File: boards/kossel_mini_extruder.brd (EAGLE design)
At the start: 66.9 x 57.9 mm, 33 parts

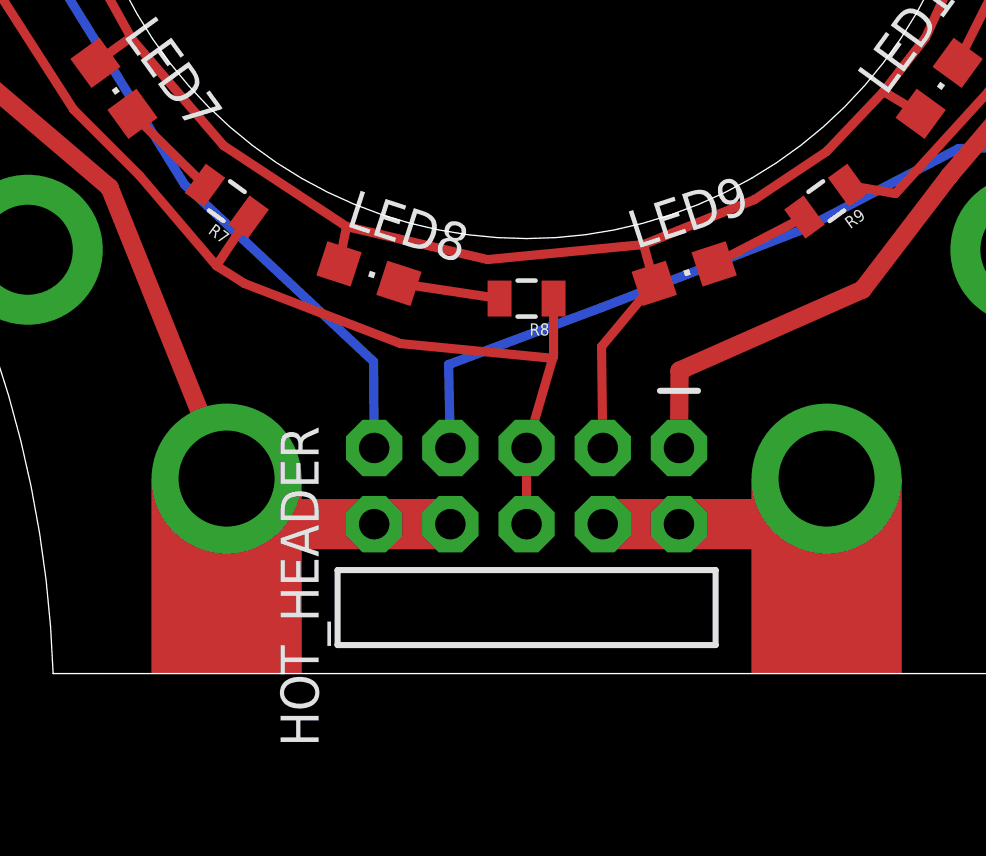
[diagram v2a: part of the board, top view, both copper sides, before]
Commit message: replaced 2x5 header with 2x4 header
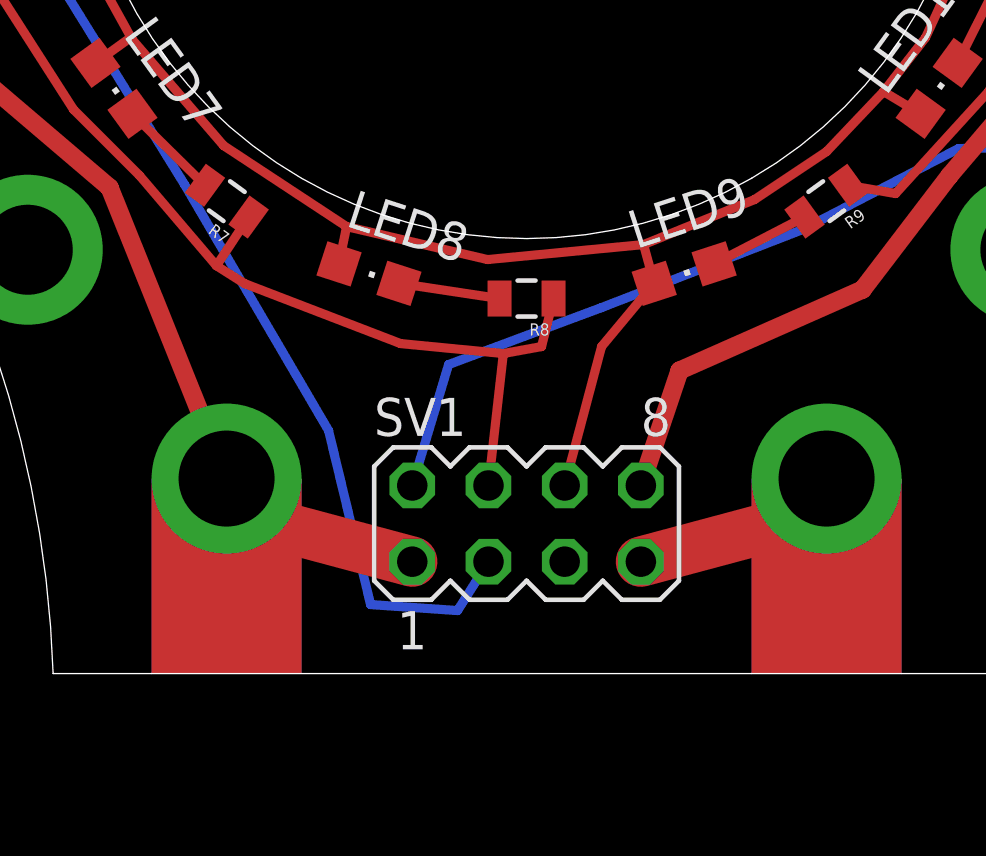
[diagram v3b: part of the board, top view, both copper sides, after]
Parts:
- removed HOT_HEADER: M05X2RA, SparkFun-Connectors:2X5-RA
- added SV1: (no value), con-lstb:MA04-2
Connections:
- net FAN_VCC: now also SV1.6; no longer HOT_HEADER.3
- net GND: now also SV1.4; no longer HOT_HEADER.5, HOT_HEADER.6
- net N$10: now also SV1.1; no longer HOT_HEADER.10, HOT_HEADER.8
- net N$11: now also SV1.3; no longer HOT_HEADER.9
- net N$12: now also SV1.2; no longer HOT_HEADER.7
- net N$15: now also SV1.7; no longer HOT_HEADER.2, HOT_HEADER.4
- net N$17: now also SV1.8; no longer HOT_HEADER.1
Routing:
- net N$11: track 49.9 -> 58.7 mm
- net GND: track 154.0 -> 152.1 mm
- net N$17: track 120.9 -> 122.4 mm
- net N$12: track 47.6 -> 49.1 mm
- net FAN_VCC: track 118.3 -> 119.7 mm
- net N$15: track 10.4 -> 9.29 mm
- net N$10: track 126.7 -> 125.5 mm
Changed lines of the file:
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@@
 <element name="R10" library="SparkFun-Passives" package="0805" value="" x="49.167959375" y="23.7467125" rot="R252"/>
 <element name="HOT_12V" library="OBKP_Effector_PCB" package="3MM" value="LUG3-X" x="23" y="6"/>
-<element name="HOT_HEADER" library="SparkFun-Connectors" package="2X5-RA" value="M05X2RA" x="33" y="5.75" rot="R270"/>
 <element name="PROBE_GND" library="OBKP_Effector_PCB" package="3MM" value="LUG3-X" x="47.9" y="49.15" rot="R120"/>
 <element name="PROBE_SIG" library="OBKP_Effector_PCB" package="3MM" value="LUG3-X" x="57.95" y="31.85" rot="R120"/>
+<element name="SV1" library="con-lstb" package="MA04-2" value="" x="33" y="4.5">
+<attribute name="OC_NEWARK" value="unknown" x="33" y="4.5" size="1.778" layer="27" display="off"/>
+<attribute name="MPN" value="" x="33" y="4.5" size="1.778" layer="27" display="off"/>
+<attribute name="MF" value="" x="33" y="4.5" size="1.778" layer="27" display="off"/>
+<attribute name="OC_FARNELL" value="unknown" x="33" y="4.5" size="1.778" layer="27" display="off"/>
+</element>
 </elements>
 <signals>
@@
 <contactref element="R8" pad="1"/>
 <contactref element="R7" pad="1"/>
-<contactref element="HOT_HEADER" pad="5"/>
-<contactref element="HOT_HEADER" pad="6"/>
 <contactref element="THERM_GND" pad="P$3"/>
 <contactref element="THERM_GND" pad="P$2"/>
@@
 <contactref element="PROBE_GND" pad="P$3"/>
 <contactref element="PROBE_GND" pad="P$2"/>
-<wire x1="33" y1="4.48" x2="33" y2="7.02" width="0.3048" layer="1"/>
-<wire x1="33" y1="7.02" x2="33.873078125" y2="10.007865625" width="0.3048" layer="1"/>
-<wire x1="33.873078125" y1="10.007865625" x2="33.9" y2="10.1" width="0.3048" layer="1"/>
-<wire x1="33.9" y1="10.1" x2="33.9" y2="12" width="0.3048" layer="1"/>
+<wire x1="33.5" y1="10.4" x2="33.9" y2="12" width="0.3048" layer="1"/>
 <wire x1="23.7357625" y1="14.717703125" x2="22.662346875" y2="13.094290625" width="0.3048" layer="1"/>
 <wire x1="22.662346875" y1="13.094290625" x2="23.6" y2="12.5" width="0.3048" layer="1"/>
 <wire x1="23.6" y1="12.5" x2="28.8" y2="10.5" width="0.3048" layer="1"/>
-<wire x1="28.8" y1="10.5" x2="33.873078125" y2="10.007865625" width="0.3048" layer="1"/>
+<wire x1="28.8" y1="10.5" x2="32.225965625" y2="10.16765" width="0.3048" layer="1"/>
 <wire x1="17.110153125" y1="22.890759375" x2="15.4" y2="22.2" width="0.3048" layer="1"/>
 <wire x1="15.4" y1="22.2" x2="17.9" y2="18.3" width="0.3048" layer="1"/>
@@
 <wire x1="8.08193125" y1="31.839365625" x2="5.267346875" y2="33.464365625" width="0.6096" layer="1"/>
 <wire x1="47.9" y1="49.15" x2="50.71458125" y2="50.775" width="0.6096" layer="1"/>
+<contactref element="SV1" pad="4"/>
+<wire x1="31.73" y1="5.77" x2="32.225965625" y2="10.16765" width="0.3048" layer="1"/>
 <wire x1="50.71458125" y1="50.775" x2="50.71458125" y2="50.775" width="0" layer="19" extent="1-16"/>
 <wire x1="5.267346875" y1="33.464365625" x2="5.267346875" y2="33.464365625" width="0" layer="19" extent="1-16"/>
+<wire x1="32.225965625" y1="10.16765" x2="33.5" y2="10.4" width="0.3048" layer="1"/>
 </signal>
 <signal name="N$7">
@@
 <contactref element="LED3" pad="A"/>
 <contactref element="LED2" pad="A"/>
-<contactref element="HOT_HEADER" pad="3"/>
 <wire x1="37.254678125" y1="12.507571875" x2="35.5" y2="10.4" width="0.3048" layer="1"/>
-<wire x1="35.5" y1="10.4" x2="35.54" y2="7.02" width="0.3048" layer="1"/>
 <wire x1="37.254678125" y1="12.507571875" x2="36.9" y2="13.8" width="0.3048" layer="1"/>
 <wire x1="36.9" y1="13.8" x2="40.6" y2="15.3" width="0.3048" layer="1"/>
@@
 <wire x1="48.4" y1="32.2" x2="47" y2="36.2" width="0.3048" layer="1"/>
 <wire x1="47" y1="36.2" x2="46.3" y2="37.5" width="0.3048" layer="1"/>
+<contactref element="SV1" pad="6"/>
+<wire x1="34.27" y1="5.77" x2="35.5" y2="10.4" width="0.3048" layer="1"/>
 </signal>
 <signal name="N$10">
-<contactref element="HOT_HEADER" pad="10"/>
 <contactref element="HOT_12V" pad="P$1"/>
 <contactref element="HOT_12V" pad="P$2"/>
 <contactref element="HOT_12V" pad="P$3"/>
-<contactref element="HOT_HEADER" pad="8"/>
-<wire x1="27.92" y1="4.48" x2="30.46" y2="4.48" width="1.6764" layer="1"/>
 <wire x1="23" y1="6" x2="19.1" y2="15.7" width="0.6096" layer="1"/>
 <contactref element="FAN_2_12V" pad="P$1"/>
@@
 <wire x1="49.9" y1="30.3" x2="49.4" y2="22.2" width="0.6096" layer="16"/>
 <wire x1="19.1" y1="15.7" x2="11.37383125" y2="22.287628125" width="0.6096" layer="1"/>
-<wire x1="23" y1="2.75" x2="23" y2="2.75" width="0" layer="19" extent="1-16"/>
-<wire x1="27.92" y1="4.48" x2="24.52" y2="4.48" width="1.6764" layer="1"/>
 <wire x1="24.52" y1="4.48" x2="23" y2="6" width="1.6764" layer="1"/>
 <wire x1="23" y1="6" x2="23" y2="2.75" width="1.6764" layer="1"/>
+<contactref element="SV1" pad="1"/>
+<wire x1="29.19" y1="3.23" x2="24.52" y2="4.48" width="1.6764" layer="1"/>
+<wire x1="23" y1="2.75" x2="23" y2="2.75" width="0" layer="19" extent="1-16"/>
 </signal>
 <signal name="N$11">
@@
 <contactref element="THERM_SIG" pad="P$2"/>
 <contactref element="THERM_SIG" pad="P$1"/>
-<contactref element="HOT_HEADER" pad="9"/>
 <wire x1="18.0814875" y1="49.15961875" x2="15.7" y2="41.3" width="0.3048" layer="1"/>
 <via x="15.7" y="41.3" extent="1-16" drill="0.9" diameter="1.778"/>
@@
 <wire x1="15.5" y1="31.1" x2="17.2" y2="22.9" width="0.3048" layer="16"/>
 <wire x1="17.2" y1="22.9" x2="21.6" y2="15.8" width="0.3048" layer="16"/>
-<wire x1="21.6" y1="15.8" x2="27.9" y2="9.9" width="0.3048" layer="16"/>
-<wire x1="27.9" y1="9.9" x2="27.92" y2="7.02" width="0.3048" layer="16"/>
+<wire x1="21.6" y1="15.8" x2="26.4" y2="7.6" width="0.3048" layer="16"/>
 <wire x1="18.0814875" y1="49.15961875" x2="15.266903125" y2="50.78461875" width="0.6096" layer="1"/>
+<contactref element="SV1" pad="3"/>
+<wire x1="26.4" y1="7.6" x2="27.8" y2="1.8" width="0.3048" layer="16"/>
+<wire x1="27.8" y1="1.8" x2="30.7" y2="1.6" width="0.3048" layer="16"/>
+<wire x1="30.7" y1="1.6" x2="31.73" y2="3.23" width="0.3048" layer="16"/>
 <wire x1="15.266903125" y1="50.78461875" x2="15.266903125" y2="50.78461875" width="0" layer="19" extent="1-16"/>
 </signal>
@@
 <contactref element="PROBE_SIG" pad="P$2"/>
 <contactref element="PROBE_SIG" pad="P$1"/>
-<contactref element="HOT_HEADER" pad="7"/>
-<wire x1="30.46" y1="7.02" x2="30.4" y2="9.8" width="0.3048" layer="16"/>
 <wire x1="30.4" y1="9.8" x2="35.5" y2="11.7" width="0.3048" layer="16"/>
 <wire x1="35.5" y1="11.7" x2="42.2" y2="14.3" width="0.3048" layer="16"/>
@@
 <wire x1="56.1" y1="27.9" x2="57.95" y2="31.85" width="0.3048" layer="1"/>
 <wire x1="57.95" y1="31.85" x2="60.76458125" y2="33.475" width="0.6096" layer="1"/>
+<contactref element="SV1" pad="2"/>
+<wire x1="30.4" y1="9.8" x2="29.19" y2="5.77" width="0.3048" layer="16"/>
 <wire x1="60.76458125" y1="33.475" x2="60.76458125" y2="33.475" width="0" layer="19" extent="1-16"/>
 </signal>
@@
 <contactref element="FAN_0_PWM" pad="P$1"/>
 <contactref element="FAN_2_PWM" pad="P$1"/>
-<contactref element="HOT_HEADER" pad="1"/>
-<wire x1="38.08" y1="7.02" x2="38.1" y2="9.6" width="0.6096" layer="1"/>
 <wire x1="38.1" y1="9.6" x2="44.2" y2="12.3" width="0.6096" layer="1"/>
 <wire x1="50.8" y1="21.3" x2="54.62690625" y2="22.28709375" width="0.6096" layer="1"/>
@@
 <wire x1="47.1" y1="16.1" x2="49.4" y2="18.8" width="0.6096" layer="1"/>
 <wire x1="49.4" y1="18.8" x2="50.8" y2="21.3" width="0.6096" layer="1"/>
+<contactref element="SV1" pad="8"/>
+<wire x1="36.81" y1="5.77" x2="38.1" y2="9.6" width="0.6096" layer="1"/>
 </signal>
 <signal name="N$15">
-<contactref element="HOT_HEADER" pad="2"/>
 <contactref element="HOT_PWM" pad="P$1"/>
 <contactref element="HOT_PWM" pad="P$2"/>
 <contactref element="HOT_PWM" pad="P$3"/>
-<contactref element="HOT_HEADER" pad="4"/>
 <wire x1="42.9999875" y1="5.9995125" x2="41.480475" y2="4.48" width="1.6764" layer="1"/>
-<wire x1="41.480475" y1="4.48" x2="38.08" y2="4.48" width="1.6764" layer="1"/>
-<wire x1="38.08" y1="4.48" x2="35.54" y2="4.48" width="1.6764" layer="1"/>
 <wire x1="41.480475" y1="4.48" x2="42.9999875" y2="2.7495125" width="0.6096" layer="1"/>
+<contactref element="SV1" pad="7"/>
+<wire x1="36.81" y1="3.23" x2="41.480475" y2="4.48" width="1.6764" layer="1"/>
 <wire x1="42.9999875" y1="2.7495125" x2="42.9999875" y2="2.7495125" width="0" layer="19" extent="1-16"/>
 </signal>

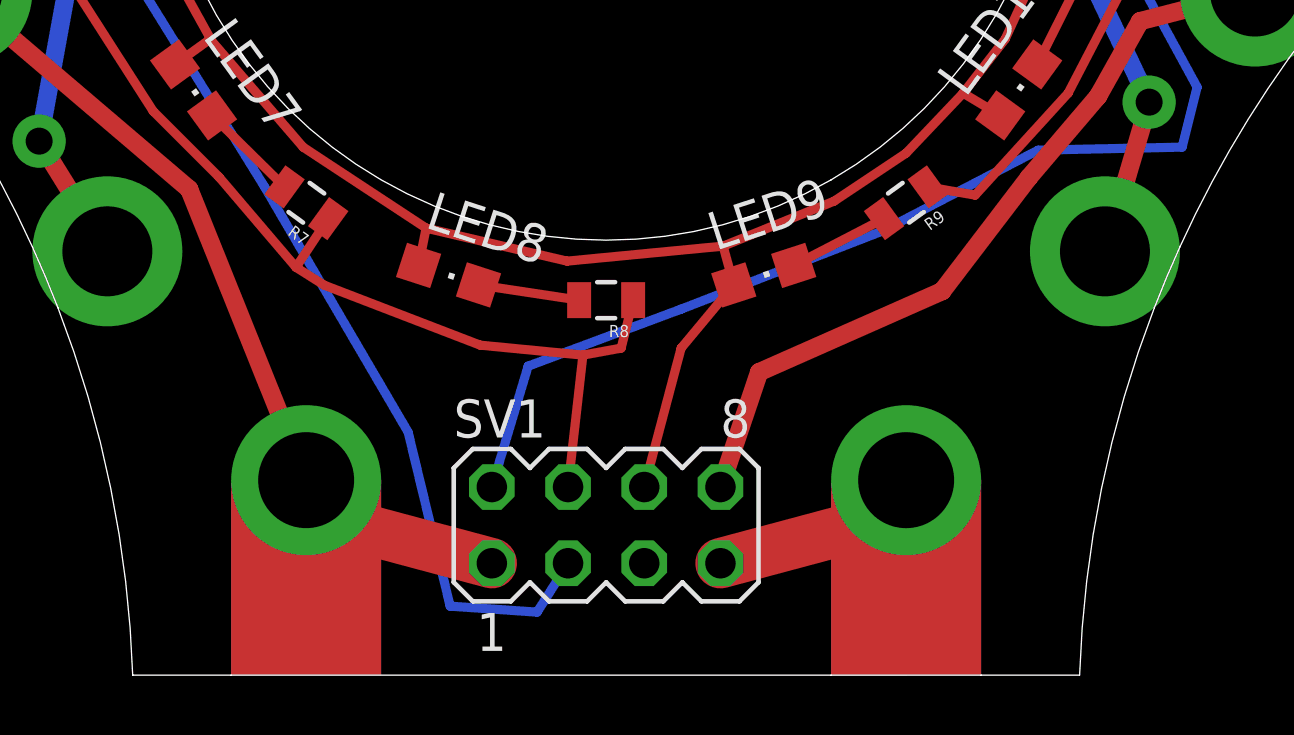
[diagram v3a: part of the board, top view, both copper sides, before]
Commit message: put fan on separate 12V supply line
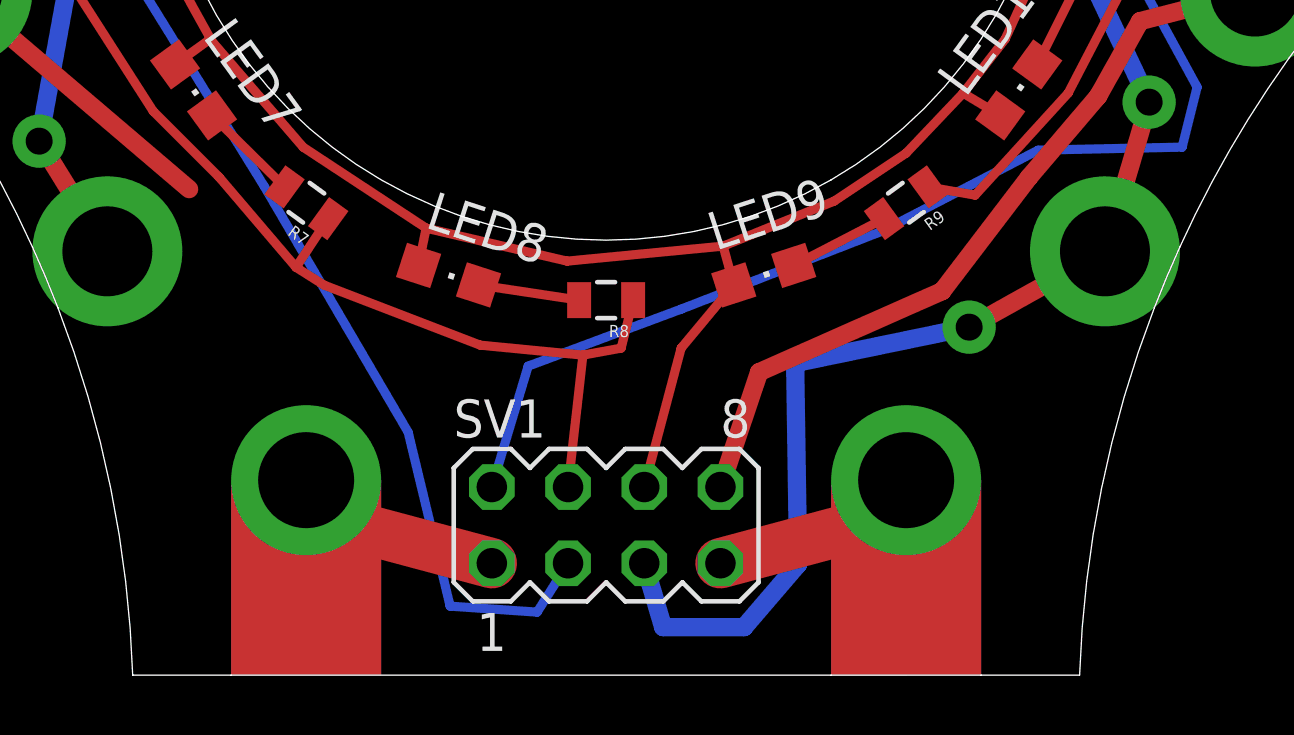
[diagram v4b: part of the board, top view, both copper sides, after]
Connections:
- removed net N$10: FAN_0_12V.P$1, FAN_1_12V.P$1, FAN_2_12V.P$1, HOT_12V.P$1, HOT_12V.P$2, HOT_12V.P$3, SV1.1
- new net FAN_12V: FAN_0_12V.P$1, FAN_1_12V.P$1, FAN_2_12V.P$1, SV1.5
- new net HOT_12V: HOT_12V.P$1, HOT_12V.P$2, HOT_12V.P$3, SV1.1
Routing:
- net FAN_12V: track 0.00 -> 130.4 mm, vias 0 -> 4
- net N$10: track 125.5 -> 0.00 mm, vias 3 -> 0
- net HOT_12V: track 0.00 -> 10.2 mm
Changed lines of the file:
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@@
 <wire x1="34.27" y1="5.77" x2="35.5" y2="10.4" width="0.3048" layer="1"/>
 </signal>
-<signal name="N$10">
-<contactref element="HOT_12V" pad="P$1"/>
-<contactref element="HOT_12V" pad="P$2"/>
-<contactref element="HOT_12V" pad="P$3"/>
-<wire x1="23" y1="6" x2="19.1" y2="15.7" width="0.6096" layer="1"/>
+<signal name="FAN_12V">
 <contactref element="FAN_2_12V" pad="P$1"/>
 <contactref element="FAN_0_12V" pad="P$1"/>
@@
 <wire x1="49.9" y1="30.3" x2="49.4" y2="22.2" width="0.6096" layer="16"/>
 <wire x1="19.1" y1="15.7" x2="11.37383125" y2="22.287628125" width="0.6096" layer="1"/>
-<wire x1="24.52" y1="4.48" x2="23" y2="6" width="1.6764" layer="1"/>
-<wire x1="23" y1="6" x2="23" y2="2.75" width="1.6764" layer="1"/>
-<contactref element="SV1" pad="1"/>
-<wire x1="29.19" y1="3.23" x2="24.52" y2="4.48" width="1.6764" layer="1"/>
-<wire x1="23" y1="2.75" x2="23" y2="2.75" width="0" layer="19" extent="1-16"/>
+<contactref element="SV1" pad="5"/>
+<wire x1="49.627128125" y1="13.626965625" x2="45.1" y2="11.1" width="0.6096" layer="1"/>
+<via x="45.1" y="11.1" extent="1-16" drill="0.9" diameter="1.778"/>
+<wire x1="45.1" y1="11.1" x2="39.3" y2="9.9" width="0.6096" layer="16"/>
+<wire x1="39.3" y1="9.9" x2="39.4" y2="3.2" width="0.6096" layer="16"/>
+<wire x1="39.4" y1="3.2" x2="37.6" y2="1.1" width="0.6096" layer="16"/>
+<wire x1="37.6" y1="1.1" x2="34.9" y2="1.1" width="0.6096" layer="16"/>
+<wire x1="34.9" y1="1.1" x2="34.27" y2="3.23" width="0.6096" layer="16"/>
 </signal>
 <signal name="N$11">
@@
 <wire x1="42.9999875" y1="2.7495125" x2="42.9999875" y2="2.7495125" width="0" layer="19" extent="1-16"/>
 </signal>
+<signal name="HOT_12V">
+<contactref element="HOT_12V" pad="P$1"/>
+<contactref element="HOT_12V" pad="P$2"/>
+<contactref element="HOT_12V" pad="P$3"/>
+<contactref element="SV1" pad="1"/>
+<wire x1="24.52" y1="4.48" x2="23" y2="6" width="1.6764" layer="1"/>
+<wire x1="23" y1="6" x2="23" y2="2.75" width="1.6764" layer="1"/>
+<wire x1="29.19" y1="3.23" x2="24.52" y2="4.48" width="1.6764" layer="1"/>
+<wire x1="23" y1="2.75" x2="23" y2="2.75" width="0" layer="19" extent="1-16"/>
+</signal>
 </signals>
-<errors>
-</errors>
 </board>
 </drawing>
